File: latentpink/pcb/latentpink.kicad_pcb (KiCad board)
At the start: 8 copper layers, 145 x 139 mm, 470 parts, among them J1 CONN_SFP_HOST, J10 XILINX_JTAG, J13 CONN_01X05, J14 CONN_01X03, J15 CONN_01X03, J16 JUMPER_0402_SPDT, J17 JUMPER_0402_SPDT, J18 BEL_FUSE_0845-2R1T-E4, J19 BEL_FUSE_0845-2R1T-E4, J2 SFP_CAGE, J20 BEL_FUSE_0845-2R1T-E4, J21 BEL_FUSE_0845-2R1T-E4, J22 BEL_FUSE_0845-2R1T-E4, J3 XILINX_JTAG, J4 BEL_FUSE_0845-2R1T-E4, J5 0826-1G1T-23-F, J6 BARREL_JACK, J7 RJ45, J8 BEL_FUSE_0845-2R1T-E4, J9 XILINX_JTAG, M1 960-27-12-D-AB-0, M2 960-23-23-F-AB-0, M3 SCREWHOLE, M4 SCREWHOLE, M5 SCREWHOLE, M6 SCREWHOLE, U1 VSC8512, U10 MYMGK1R812ERSR, U11 MYMGK00504ERSR, U12 STM32L031-QFN32, U13 MYMGK00504ERSR, U14 MYMGK00504ERSR, U15 MYMGK00504ERSR, U16 NCP45521IMNTWG-H, U17 NCP45521IMNTWG-H, U18 LP2996AMRE, U19 TPS7A2533DRVR, U2 XC7K160T-2FBG484C, U20 AT24MAC402, U21 ECX2-LMV-3CN-125.000-TR, U22 ECS-2016MVQ-250-CN, U3 CY7C2245KV18-450BZXI, U4 STM32H735-UFBGA176-25, U5 DP83867, U6 DP83867, U9 KSZ9031RN

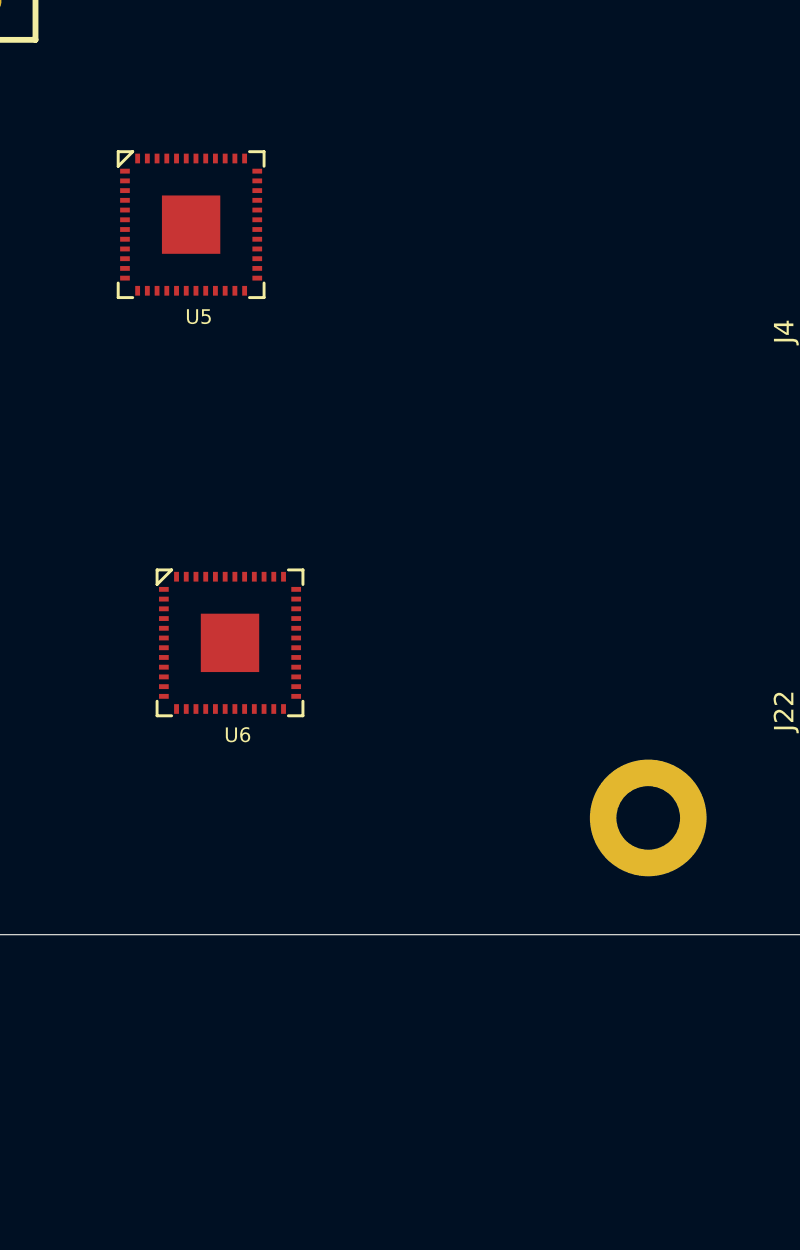
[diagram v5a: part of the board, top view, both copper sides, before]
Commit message: Initial start of DP83867 schematic
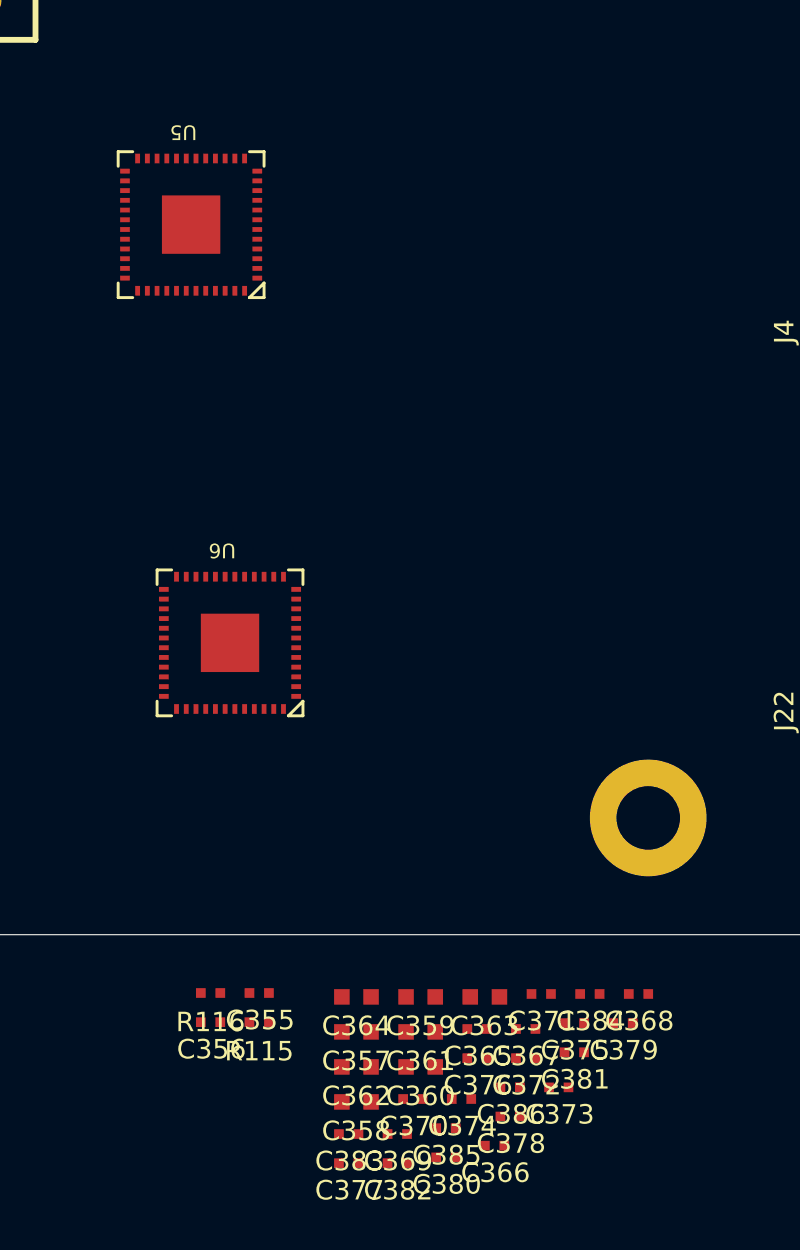
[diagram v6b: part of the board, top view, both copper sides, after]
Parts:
- added C355: 0.47 uF, azonenberg_pcb:EIA_0402_CAP_NOSILK, F.Cu at (121.0, 163.0)
- added C356: 0.47 uF, azonenberg_pcb:EIA_0402_CAP_NOSILK, F.Cu at (118.5, 164.5)
- added C357: 4.7 uF, azonenberg_pcb:EIA_0603_CAP_NOSILK, F.Cu at (126.0, 165.0)
- added C358: 4.7 uF, azonenberg_pcb:EIA_0603_CAP_NOSILK, F.Cu at (126.0, 168.6)
- added C359: 4.7 uF, azonenberg_pcb:EIA_0603_CAP_NOSILK, F.Cu at (129.3, 163.2)
- added C360: 4.7 uF, azonenberg_pcb:EIA_0603_CAP_NOSILK, F.Cu at (129.3, 166.8)
- added C361: 4.7 uF, azonenberg_pcb:EIA_0603_CAP_NOSILK, F.Cu at (129.3, 165.0)
- added C362: 4.7 uF, azonenberg_pcb:EIA_0603_CAP_NOSILK, F.Cu at (126.0, 166.8)
- added C363: 4.7 uF, azonenberg_pcb:EIA_0603_CAP_NOSILK, F.Cu at (132.6, 163.2)
- added C364: 4.7 uF, azonenberg_pcb:EIA_0603_CAP_NOSILK, F.Cu at (126.0, 163.2)
- added C365: 0.47 uF, azonenberg_pcb:EIA_0402_CAP_NOSILK, F.Cu at (132.2, 164.8)
- added C366: 0.47 uF, azonenberg_pcb:EIA_0402_CAP_NOSILK, F.Cu at (133.1, 170.8)
- added C367: 0.47 uF, azonenberg_pcb:EIA_0402_CAP_NOSILK, F.Cu at (134.7, 164.8)
- added C368: 0.47 uF, azonenberg_pcb:EIA_0402_CAP_NOSILK, F.Cu at (140.5, 163.1)
- added C369: 0.47 uF, azonenberg_pcb:EIA_0402_CAP_NOSILK, F.Cu at (128.1, 170.2)
- added C370: 0.47 uF, azonenberg_pcb:EIA_0402_CAP_NOSILK, F.Cu at (128.9, 168.4)
- added C371: 0.47 uF, azonenberg_pcb:EIA_0402_CAP_NOSILK, F.Cu at (135.5, 163.1)
- added C372: 0.47 uF, azonenberg_pcb:EIA_0402_CAP_NOSILK, F.Cu at (134.7, 166.3)
- added C373: 0.47 uF, azonenberg_pcb:EIA_0402_CAP_NOSILK, F.Cu at (136.4, 167.8)
- added C374: 0.47 uF, azonenberg_pcb:EIA_0402_CAP_NOSILK, F.Cu at (131.4, 168.4)
- added C375: 0.47 uF, azonenberg_pcb:EIA_0402_CAP_NOSILK, F.Cu at (137.2, 164.6)
- added C376: 0.47 uF, azonenberg_pcb:EIA_0402_CAP_NOSILK, F.Cu at (132.2, 166.3)
- added C377: 0.47 uF, azonenberg_pcb:EIA_0402_CAP_NOSILK, F.Cu at (125.6, 171.8)
- added C378: 0.47 uF, azonenberg_pcb:EIA_0402_CAP_NOSILK, F.Cu at (133.9, 169.3)
- added C379: 0.47 uF, azonenberg_pcb:EIA_0402_CAP_NOSILK, F.Cu at (139.7, 164.6)
- added C380: 0.47 uF, azonenberg_pcb:EIA_0402_CAP_NOSILK, F.Cu at (130.6, 171.4)
- added C381: 0.47 uF, azonenberg_pcb:EIA_0402_CAP_NOSILK, F.Cu at (137.2, 166.1)
- added C382: 0.47 uF, azonenberg_pcb:EIA_0402_CAP_NOSILK, F.Cu at (128.1, 171.8)
- added C383: 0.47 uF, azonenberg_pcb:EIA_0402_CAP_NOSILK, F.Cu at (125.6, 170.2)
- added C384: 0.47 uF, azonenberg_pcb:EIA_0402_CAP_NOSILK, F.Cu at (138.0, 163.1)
- added C385: 0.47 uF, azonenberg_pcb:EIA_0402_CAP_NOSILK, F.Cu at (130.6, 169.9)
- added C386: 0.47 uF, azonenberg_pcb:EIA_0402_CAP_NOSILK, F.Cu at (133.9, 167.8)
- added R115: 33, azonenberg_pcb:EIA_0402_RES_NOSILK, F.Cu at (121.0, 164.5)
- added R116: 33, azonenberg_pcb:EIA_0402_RES_NOSILK, F.Cu at (118.5, 163.0)
- turned U5 to 180 degrees
- turned U6 to 180 degrees
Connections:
- J18 pad SHLD: /QSGMII PHY/CHGND -> /CHGND
- J19 pad SHLD: /QSGMII PHY/CHGND -> /CHGND
- J20 pad SHLD: /QSGMII PHY/CHGND -> /CHGND
- J21 pad SHLD: /QSGMII PHY/CHGND -> /CHGND
- J22 pad 1: unconnected-(J22-Pad1) -> /GND
- J22 pad 10: unconnected-(J22-Pad10) -> /SGMII PHYs/ETH13_C_N
- J22 pad 11: unconnected-(J22-Pad11) -> /SGMII PHYs/ETH13_B_P
- J22 pad 13: unconnected-(J22-Pad13) -> /SGMII PHYs/ETH13_A_N
- J22 pad 15: unconnected-(J22-Pad15) -> /SGMII PHYs/ETH12_A_N
- J22 pad 16: unconnected-(J22-Pad16) -> /SGMII PHYs/ETH12_B_N
- J22 pad 18: unconnected-(J22-Pad18) -> /SGMII PHYs/ETH12_C_P
- J22 pad 19: unconnected-(J22-Pad19) -> /SGMII PHYs/ETH12_D_N
- J22 pad 2: unconnected-(J22-Pad2) -> /SGMII PHYs/ETH13_D_N
- J22 pad 20: unconnected-(J22-Pad20) -> /GND
- J22 pad 21: unconnected-(J22-Pad21) -> /SGMII PHYs/ETH12_A_N
- J22 pad 23: unconnected-(J22-Pad23) -> /SGMII PHYs/ETH12_B_P
- J22 pad 24: unconnected-(J22-Pad24) -> /SGMII PHYs/ETH12_C_N
- J22 pad 26: unconnected-(J22-Pad26) -> /SGMII PHYs/ETH12_D_P
- J22 pad 3: unconnected-(J22-Pad3) -> /SGMII PHYs/ETH13_C_P
- J22 pad 5: unconnected-(J22-Pad5) -> /SGMII PHYs/ETH13_B_N
- J22 pad 6: unconnected-(J22-Pad6) -> /SGMII PHYs/ETH13_A_P
- J22 pad 9: unconnected-(J22-Pad9) -> /SGMII PHYs/ETH13_D_P
- J22 pad SHLD: unconnected-(J22-PadSHLD) -> /CHGND
- J4 pad SHLD: /QSGMII PHY/CHGND -> /CHGND
- J8 pad SHLD: /QSGMII PHY/CHGND -> /CHGND
- U2 pad AA5: unconnected-(U2-PadAA5) -> /SGMII PHYs/ETH13_INT_N
- U2 pad AA6: unconnected-(U2-PadAA6) -> /SGMII PHYs/DP_MDC
- U2 pad AB5: unconnected-(U2-PadAB5) -> /SGMII PHYs/ETH13_RST_N
- U2 pad AB6: unconnected-(U2-PadAB6) -> /SGMII PHYs/DP_MDIO
- U2 pad AB7: unconnected-(U2-PadAB7) -> /SGMII PHYs/ETH12_RST_N
- U2 pad AB8: unconnected-(U2-PadAB8) -> /SGMII PHYs/ETH12_INT_N
- U2 pad T14: unconnected-(U2-PadT14) -> Net-(U2-PadT14)
- U2 pad T6: unconnected-(U2-PadT6) -> Net-(U2-PadT6)
- U5 pad 1: unconnected-(U5-Pad1) -> /SGMII PHYs/ETH13_A_P
- U5 pad 10: unconnected-(U5-Pad10) -> /SGMII PHYs/ETH13_D_P
- U5 pad 11: unconnected-(U5-Pad11) -> /SGMII PHYs/ETH13_D_N
- U5 pad 12: unconnected-(U5-Pad12) -> Net-(U5-Pad12)
- U5 pad 13: unconnected-(U5-Pad13) -> /SGMII PHYs/DP_A1V8
- U5 pad 15: unconnected-(U5-Pad15) -> /SGMII PHYs/PHY_CLK_25MHZ_1
- U5 pad 16: unconnected-(U5-Pad16) -> /SGMII PHYs/DP_MDC
- U5 pad 17: unconnected-(U5-Pad17) -> /SGMII PHYs/DP_MDIO
- U5 pad 18: unconnected-(U5-Pad18) -> /SGMII PHYs/DP_CLKOUT1
- U5 pad 19: unconnected-(U5-Pad19) -> /1V8
- U5 pad 2: unconnected-(U5-Pad2) -> /SGMII PHYs/ETH13_A_N
- U5 pad 24: unconnected-(U5-Pad24) -> /1V0
- U5 pad 27: unconnected-(U5-Pad27) -> /SGMII PHYs/ETH13_SGMII_TX_P
- U5 pad 28: unconnected-(U5-Pad28) -> /SGMII PHYs/ETH13_SGMII_TX_N
- U5 pad 3: unconnected-(U5-Pad3) -> /SGMII PHYs/DP_A2V5
- U5 pad 30: unconnected-(U5-Pad30) -> /1V8
- U5 pad 31: unconnected-(U5-Pad31) -> /1V0
- U5 pad 33: unconnected-(U5-Pad33) -> /SGMII PHYs/ETH13_SGMII_CLKOUT_P
- U5 pad 34: unconnected-(U5-Pad34) -> /SGMII PHYs/ETH13_SGMII_CLKOUT_N
- U5 pad 35: unconnected-(U5-Pad35) -> /SGMII PHYs/ETH13_SGMII_RX_P
- U5 pad 36: unconnected-(U5-Pad36) -> /SGMII PHYs/ETH13_SGMII_RX_N
- U5 pad 38: unconnected-(U5-Pad38) -> /SGMII PHYs/ETH13_RX_CTRL_STRAP
- U5 pad 4: unconnected-(U5-Pad4) -> /SGMII PHYs/ETH13_B_P
- U5 pad 41: unconnected-(U5-Pad41) -> /1V8
- U5 pad 42: unconnected-(U5-Pad42) -> /1V0
- U5 pad 43: unconnected-(U5-Pad43) -> /SGMII PHYs/ETH13_RST_N
- U5 pad 44: unconnected-(U5-Pad44) -> /SGMII PHYs/ETH13_INT_N
- U5 pad 48: unconnected-(U5-Pad48) -> /SGMII PHYs/DP_A1V8
- U5 pad 5: unconnected-(U5-Pad5) -> /SGMII PHYs/ETH13_B_N
- U5 pad 6: unconnected-(U5-Pad6) -> /1V0
- U5 pad 7: unconnected-(U5-Pad7) -> /SGMII PHYs/ETH13_C_P
- U5 pad 8: unconnected-(U5-Pad8) -> /SGMII PHYs/ETH13_C_N
- U5 pad 9: unconnected-(U5-Pad9) -> /SGMII PHYs/DP_A2V5
- U5 pad PAD: unconnected-(U5-PadPAD) -> /GND
- U6 pad 1: unconnected-(U6-Pad1) -> /SGMII PHYs/ETH12_A_P
- U6 pad 10: unconnected-(U6-Pad10) -> /SGMII PHYs/ETH12_D_P
- U6 pad 11: unconnected-(U6-Pad11) -> /SGMII PHYs/ETH12_D_N
- U6 pad 12: unconnected-(U6-Pad12) -> Net-(U6-Pad12)
- U6 pad 13: unconnected-(U6-Pad13) -> /SGMII PHYs/DP_A1V8
- U6 pad 15: unconnected-(U6-Pad15) -> /SGMII PHYs/PHY_CLK_25MHZ_0
- U6 pad 16: unconnected-(U6-Pad16) -> /SGMII PHYs/DP_MDC
- U6 pad 17: unconnected-(U6-Pad17) -> /SGMII PHYs/DP_MDIO
- U6 pad 18: unconnected-(U6-Pad18) -> /SGMII PHYs/DP_CLKOUT0
- U6 pad 19: unconnected-(U6-Pad19) -> /1V8
- U6 pad 2: unconnected-(U6-Pad2) -> /SGMII PHYs/ETH12_A_N
- U6 pad 24: unconnected-(U6-Pad24) -> /1V0
- U6 pad 27: unconnected-(U6-Pad27) -> /SGMII PHYs/ETH12_SGMII_TX_P
- U6 pad 28: unconnected-(U6-Pad28) -> /SGMII PHYs/ETH12_SGMII_TX_N
- U6 pad 3: unconnected-(U6-Pad3) -> /SGMII PHYs/DP_A2V5
- U6 pad 30: unconnected-(U6-Pad30) -> /1V8
- U6 pad 31: unconnected-(U6-Pad31) -> /1V0
- U6 pad 33: unconnected-(U6-Pad33) -> /SGMII PHYs/ETH12_SGMII_CLKOUT_P
- U6 pad 34: unconnected-(U6-Pad34) -> /SGMII PHYs/ETH12_SGMII_CLKOUT_N
- U6 pad 35: unconnected-(U6-Pad35) -> /SGMII PHYs/ETH12_SGMII_RX_P
- U6 pad 36: unconnected-(U6-Pad36) -> /SGMII PHYs/ETH12_SGMII_RX_N
- U6 pad 38: unconnected-(U6-Pad38) -> /SGMII PHYs/ETH12_RX_CTRL_STRAP
- U6 pad 4: unconnected-(U6-Pad4) -> /SGMII PHYs/ETH12_B_P
- U6 pad 41: unconnected-(U6-Pad41) -> /1V8
- U6 pad 42: unconnected-(U6-Pad42) -> /1V0
- U6 pad 43: unconnected-(U6-Pad43) -> /SGMII PHYs/ETH12_RST_N
- U6 pad 44: unconnected-(U6-Pad44) -> /SGMII PHYs/ETH12_INT_N
- U6 pad 48: unconnected-(U6-Pad48) -> /SGMII PHYs/DP_A1V8
- U6 pad 5: unconnected-(U6-Pad5) -> /SGMII PHYs/ETH12_B_N
- U6 pad 6: unconnected-(U6-Pad6) -> /1V0
- U6 pad 7: unconnected-(U6-Pad7) -> /SGMII PHYs/ETH12_C_P
- U6 pad 8: unconnected-(U6-Pad8) -> /SGMII PHYs/ETH12_C_N
- U6 pad 9: unconnected-(U6-Pad9) -> /SGMII PHYs/DP_A2V5
- U6 pad PAD: unconnected-(U6-PadPAD) -> /GND

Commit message: Rearranged ports, added center tap capacitors
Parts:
- added C387: 0.1 uF, azonenberg_pcb:EIA_0402_CAP_NOSILK, F.Cu at (118.5, 47.0)
- added C388: 0.1 uF, azonenberg_pcb:EIA_0402_CAP_NOSILK, F.Cu at (113.5, 47.0)
- added C389: 0.1 uF, azonenberg_pcb:EIA_0402_CAP_NOSILK, F.Cu at (113.5, 48.5)
- added C390: 0.1 uF, azonenberg_pcb:EIA_0402_CAP_NOSILK, F.Cu at (116.0, 48.5)
- added C391: 0.1 uF, azonenberg_pcb:EIA_0402_CAP_NOSILK, F.Cu at (116.0, 47.0)
- added C392: 0.1 uF, azonenberg_pcb:EIA_0402_CAP_NOSILK, F.Cu at (118.5, 48.5)
- added C393: 0.1 uF, azonenberg_pcb:EIA_0402_CAP_NOSILK, F.Cu at (202.5, 31.0)
- added C394: 0.1 uF, azonenberg_pcb:EIA_0402_CAP_NOSILK, F.Cu at (195.0, 31.0)
- added C395: 0.1 uF, azonenberg_pcb:EIA_0402_CAP_NOSILK, F.Cu at (192.5, 34.0)
- added C396: 0.1 uF, azonenberg_pcb:EIA_0402_CAP_NOSILK, F.Cu at (207.5, 26.5)
- added C397: 0.1 uF, azonenberg_pcb:EIA_0402_CAP_NOSILK, F.Cu at (192.5, 32.5)
- added C398: 0.1 uF, azonenberg_pcb:EIA_0402_CAP_NOSILK, F.Cu at (192.5, 26.5)
- added C399: 0.1 uF, azonenberg_pcb:EIA_0402_CAP_NOSILK, F.Cu at (195.0, 28.0)
- added C400: 0.1 uF, azonenberg_pcb:EIA_0402_CAP_NOSILK, F.Cu at (200.0, 32.5)
- added C401: 0.1 uF, azonenberg_pcb:EIA_0402_CAP_NOSILK, F.Cu at (205.0, 26.5)
- added C402: 0.1 uF, azonenberg_pcb:EIA_0402_CAP_NOSILK, F.Cu at (197.5, 35.5)
- added C403: 0.1 uF, azonenberg_pcb:EIA_0402_CAP_NOSILK, F.Cu at (197.5, 32.5)
- added C404: 0.1 uF, azonenberg_pcb:EIA_0402_CAP_NOSILK, F.Cu at (202.5, 34.0)
- added C405: 0.1 uF, azonenberg_pcb:EIA_0402_CAP_NOSILK, F.Cu at (200.0, 29.5)
- added C406: 0.1 uF, azonenberg_pcb:EIA_0402_CAP_NOSILK, F.Cu at (195.0, 34.0)
- added C407: 0.1 uF, azonenberg_pcb:EIA_0402_CAP_NOSILK, F.Cu at (197.5, 31.0)
- added C408: 0.1 uF, azonenberg_pcb:EIA_0402_CAP_NOSILK, F.Cu at (197.5, 26.5)
- added C409: 0.1 uF, azonenberg_pcb:EIA_0402_CAP_NOSILK, F.Cu at (205.0, 28.0)
- added C410: 0.1 uF, azonenberg_pcb:EIA_0402_CAP_NOSILK, F.Cu at (195.0, 26.5)
- added C411: 0.1 uF, azonenberg_pcb:EIA_0402_CAP_NOSILK, F.Cu at (200.0, 28.0)
- added C412: 0.1 uF, azonenberg_pcb:EIA_0402_CAP_NOSILK, F.Cu at (195.0, 35.5)
- added C413: 0.1 uF, azonenberg_pcb:EIA_0402_CAP_NOSILK, F.Cu at (197.5, 37.0)
- added C414: 0.1 uF, azonenberg_pcb:EIA_0402_CAP_NOSILK, F.Cu at (200.0, 34.0)
- added C415: 0.1 uF, azonenberg_pcb:EIA_0402_CAP_NOSILK, F.Cu at (195.0, 37.0)
- added C416: 0.1 uF, azonenberg_pcb:EIA_0402_CAP_NOSILK, F.Cu at (202.5, 28.0)
- added C417: 0.1 uF, azonenberg_pcb:EIA_0402_CAP_NOSILK, F.Cu at (207.5, 28.0)
- added C418: 0.1 uF, azonenberg_pcb:EIA_0402_CAP_NOSILK, F.Cu at (195.0, 29.5)
- added C419: 0.1 uF, azonenberg_pcb:EIA_0402_CAP_NOSILK, F.Cu at (205.0, 31.0)
- added C420: 0.1 uF, azonenberg_pcb:EIA_0402_CAP_NOSILK, F.Cu at (192.5, 28.0)
- added C421: 0.1 uF, azonenberg_pcb:EIA_0402_CAP_NOSILK, F.Cu at (192.5, 35.5)
- added C422: 0.1 uF, azonenberg_pcb:EIA_0402_CAP_NOSILK, F.Cu at (210.0, 26.5)
- added C423: 0.1 uF, azonenberg_pcb:EIA_0402_CAP_NOSILK, F.Cu at (192.5, 29.5)
- added C424: 0.1 uF, azonenberg_pcb:EIA_0402_CAP_NOSILK, F.Cu at (192.5, 31.0)
- added C425: 0.1 uF, azonenberg_pcb:EIA_0402_CAP_NOSILK, F.Cu at (202.5, 29.5)
- added C426: 0.1 uF, azonenberg_pcb:EIA_0402_CAP_NOSILK, F.Cu at (202.5, 32.5)
- added C427: 0.1 uF, azonenberg_pcb:EIA_0402_CAP_NOSILK, F.Cu at (197.5, 29.5)
- added C428: 0.1 uF, azonenberg_pcb:EIA_0402_CAP_NOSILK, F.Cu at (205.0, 29.5)
- added C429: 0.1 uF, azonenberg_pcb:EIA_0402_CAP_NOSILK, F.Cu at (197.5, 34.0)
- added C430: 0.1 uF, azonenberg_pcb:EIA_0402_CAP_NOSILK, F.Cu at (197.5, 28.0)
- added C431: 0.1 uF, azonenberg_pcb:EIA_0402_CAP_NOSILK, F.Cu at (207.5, 29.5)
- added C432: 0.1 uF, azonenberg_pcb:EIA_0402_CAP_NOSILK, F.Cu at (210.0, 28.0)
- added C433: 0.1 uF, azonenberg_pcb:EIA_0402_CAP_NOSILK, F.Cu at (202.5, 26.5)
- added C434: 0.1 uF, azonenberg_pcb:EIA_0402_CAP_NOSILK, F.Cu at (205.0, 32.5)
- added C435: 0.1 uF, azonenberg_pcb:EIA_0402_CAP_NOSILK, F.Cu at (192.5, 37.0)
- added C436: 0.1 uF, azonenberg_pcb:EIA_0402_CAP_NOSILK, F.Cu at (200.0, 35.5)
- added C437: 0.1 uF, azonenberg_pcb:EIA_0402_CAP_NOSILK, F.Cu at (195.0, 32.5)
- added C438: 0.1 uF, azonenberg_pcb:EIA_0402_CAP_NOSILK, B.Cu at (153.8, 54.5)
- added C439: 0.1 uF, azonenberg_pcb:EIA_0402_CAP_NOSILK, F.Cu at (200.0, 37.0)
- added C440: 0.1 uF, azonenberg_pcb:EIA_0402_CAP_NOSILK, B.Cu at (153.8, 48.5)
- added U23: ADM3101E_QFN, azonenberg_pcb:QFN_12_0.5MM_3x3MM, F.Cu at (64.0, 70.0)
- R100, R103, R82, R85, R87, R90, R91, R94, R99: moved to B.Cu
- moved J15 193.2 mm to (76.5, 136.5)
- moved C360 141.1 mm to (110.2, 26.9)
- moved C362 141.1 mm to (106.9, 26.9)
- moved C368 141.1 mm to (121.4, 23.2)
- moved C371 141.1 mm to (116.4, 23.2)
- moved C375 141.1 mm to (118.1, 24.7)
- moved C379 141.1 mm to (120.6, 24.7)
- moved C381 141.1 mm to (118.1, 26.2)
- moved C384 141.1 mm to (118.9, 23.2)
- moved C355 141.1 mm to (101.9, 23.1)
- moved C356 141.1 mm to (99.4, 24.6)
- moved C357 141.1 mm to (106.9, 25.1)
- moved C358 141.1 mm to (106.9, 28.8)
- moved C359 141.1 mm to (110.2, 23.4)
- moved C361 141.1 mm to (110.2, 25.1)
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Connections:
- C355 pad 1: /1V8 -> /SGMII PHYs/1V8_IO
- C356 pad 1: /1V8 -> /SGMII PHYs/1V8_IO
- C360 pad 1: /SGMII PHYs/D1V8 -> /SGMII PHYs/1V8_IO
- C364 pad 1: /SGMII PHYs/D1V8 -> /SGMII PHYs/1V8_IO
- C368 pad 1: /SGMII PHYs/D1V8 -> /SGMII PHYs/1V8_IO
- C372 pad 1: /SGMII PHYs/D1V8 -> /SGMII PHYs/1V8_IO
- C375 pad 1: /SGMII PHYs/D1V8 -> /SGMII PHYs/1V8_IO
- C378 pad 1: /SGMII PHYs/D1V8 -> /SGMII PHYs/1V8_IO
- C382 pad 1: /SGMII PHYs/D1V8 -> /SGMII PHYs/1V8_IO
- C384 pad 1: /SGMII PHYs/D1V8 -> /SGMII PHYs/1V8_IO
- J18 pad 12: unconnected-(J18-Pad12) -> /QSGMII PHY/ETH4_TAP_1
- J18 pad 14: unconnected-(J18-Pad14) -> /QSGMII PHY/ETH5_TAP_0
- J18 pad 17: unconnected-(J18-Pad17) -> /QSGMII PHY/ETH5_TAP_2
- J18 pad 22: unconnected-(J18-Pad22) -> /QSGMII PHY/ETH5_TAP_1
- J18 pad 25: unconnected-(J18-Pad25) -> /QSGMII PHY/ETH5_TAP_3
- J18 pad 4: unconnected-(J18-Pad4) -> /QSGMII PHY/ETH4_TAP_2
- J18 pad 7: unconnected-(J18-Pad7) -> /QSGMII PHY/ETH4_TAP_0
- J18 pad 8: unconnected-(J18-Pad8) -> /QSGMII PHY/ETH4_TAP_3
- J19 pad 12: unconnected-(J19-Pad12) -> /QSGMII PHY/ETH6_TAP_1
- J19 pad 14: unconnected-(J19-Pad14) -> /QSGMII PHY/ETH7_TAP_0
- J19 pad 17: unconnected-(J19-Pad17) -> /QSGMII PHY/ETH7_TAP_2
- J19 pad 22: unconnected-(J19-Pad22) -> /QSGMII PHY/ETH7_TAP_1
- J19 pad 25: unconnected-(J19-Pad25) -> /QSGMII PHY/ETH7_TAP_3
- J19 pad 4: unconnected-(J19-Pad4) -> /QSGMII PHY/ETH6_TAP_2
- J19 pad 7: unconnected-(J19-Pad7) -> /QSGMII PHY/ETH6_TAP_0
- J19 pad 8: unconnected-(J19-Pad8) -> /QSGMII PHY/ETH6_TAP_3
- J20 pad 12: unconnected-(J20-Pad12) -> /QSGMII PHY/ETH8_TAP_1
- J20 pad 14: unconnected-(J20-Pad14) -> /QSGMII PHY/ETH9_TAP_0
- J20 pad 17: unconnected-(J20-Pad17) -> /QSGMII PHY/ETH9_TAP_2
- J20 pad 22: unconnected-(J20-Pad22) -> /QSGMII PHY/ETH9_TAP_1
- J20 pad 25: unconnected-(J20-Pad25) -> /QSGMII PHY/ETH9_TAP_3
- J20 pad 4: unconnected-(J20-Pad4) -> /QSGMII PHY/ETH8_TAP_2
- J20 pad 7: unconnected-(J20-Pad7) -> /QSGMII PHY/ETH8_TAP_0
- J20 pad 8: unconnected-(J20-Pad8) -> /QSGMII PHY/ETH8_TAP_3
- J21 pad 12: unconnected-(J21-Pad12) -> /QSGMII PHY/ETH10_TAP_1
- J21 pad 14: unconnected-(J21-Pad14) -> /QSGMII PHY/ETH11_TAP_0
- J21 pad 17: unconnected-(J21-Pad17) -> /QSGMII PHY/ETH11_TAP_2
- J21 pad 22: unconnected-(J21-Pad22) -> /QSGMII PHY/ETH11_TAP_1
- J21 pad 25: unconnected-(J21-Pad25) -> /QSGMII PHY/ETH11_TAP_3
- J21 pad 4: unconnected-(J21-Pad4) -> /QSGMII PHY/ETH10_TAP_2
- J21 pad 7: unconnected-(J21-Pad7) -> /QSGMII PHY/ETH10_TAP_0
- J21 pad 8: unconnected-(J21-Pad8) -> /QSGMII PHY/ETH10_TAP_3
- J4 pad 12: unconnected-(J4-Pad12) -> /QSGMII PHY/ETH0_TAP_1
- J4 pad 14: unconnected-(J4-Pad14) -> /QSGMII PHY/ETH1_TAP_0
- J4 pad 17: unconnected-(J4-Pad17) -> /QSGMII PHY/ETH1_TAP_2
- J4 pad 22: unconnected-(J4-Pad22) -> /QSGMII PHY/ETH1_TAP_1
- J4 pad 25: unconnected-(J4-Pad25) -> /QSGMII PHY/ETH1_TAP_3
- J4 pad 4: unconnected-(J4-Pad4) -> /QSGMII PHY/ETH0_TAP_2
- J4 pad 7: unconnected-(J4-Pad7) -> /QSGMII PHY/ETH0_TAP_0
- J4 pad 8: unconnected-(J4-Pad8) -> /QSGMII PHY/ETH0_TAP_3
- J8 pad 12: unconnected-(J8-Pad12) -> /QSGMII PHY/ETH2_TAP_1
- J8 pad 14: unconnected-(J8-Pad14) -> /QSGMII PHY/ETH3_TAP_0
- J8 pad 17: unconnected-(J8-Pad17) -> /QSGMII PHY/ETH3_TAP_2
- J8 pad 22: unconnected-(J8-Pad22) -> /QSGMII PHY/ETH3_TAP_1
- J8 pad 25: unconnected-(J8-Pad25) -> /QSGMII PHY/ETH3_TAP_3
- J8 pad 4: unconnected-(J8-Pad4) -> /QSGMII PHY/ETH2_TAP_2
- J8 pad 7: unconnected-(J8-Pad7) -> /QSGMII PHY/ETH2_TAP_0
- J8 pad 8: unconnected-(J8-Pad8) -> /QSGMII PHY/ETH2_TAP_3
- U2 pad U6: unconnected-(U2-PadU6) -> /SGMII PHYs/ETH12_SGMII_RX_AC_N
- U2 pad U7: unconnected-(U2-PadU7) -> /SGMII PHYs/ETH12_SGMII_RX_AC_P
- U2 pad V7: unconnected-(U2-PadV7) -> /SGMII PHYs/ETH12_SGMII_TX_AC_P
- U2 pad W7: unconnected-(U2-PadW7) -> /SGMII PHYs/ETH12_SGMII_TX_AC_N
- U2 pad Y7: unconnected-(U2-PadY7) -> /SGMII PHYs/ETH12_SGMII_CLKOUT_AC_N
- U2 pad Y8: unconnected-(U2-PadY8) -> /SGMII PHYs/ETH12_SGMII_CLKOUT_AC_P
- U5 pad 19: /1V8 -> /SGMII PHYs/1V8_IO
- U5 pad 30: /1V8 -> /SGMII PHYs/1V8_IO
- U5 pad 41: /1V8 -> /SGMII PHYs/1V8_IO
- U6 pad 19: /1V8 -> /SGMII PHYs/1V8_IO
- U6 pad 30: /1V8 -> /SGMII PHYs/1V8_IO
- U6 pad 41: /1V8 -> /SGMII PHYs/1V8_IO
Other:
- board text added: "3V3_SB"
- board text added: "FPGA JTAG 1.8V"
- board text added: "GND"
- board text added: "MCU JTAG 3.3V"
- board text added: "PHY JTAG 2.5V"
- board text added: "RST#"
- board text added: "RX"
- board text added: "SUPER SWD 3.3V"
- board text added: "SUPER UART 3.3V"
- board text added: "SWCLK"
- board text added: "SWDIO"
- board text added: "TX"

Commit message: Continued initial component placement
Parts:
- removed C229: 0.1 uF, azonenberg_pcb:EIA_0402_CAP_NOSILK
- removed R53: 1M, azonenberg_pcb:EIA_0402_RES_NOSILK
- added C441: 0.1 uF, azonenberg_pcb:EIA_0402_CAP_NOSILK, F.Cu at (122.4, 51.1)
- added C442: 0.1 uF, azonenberg_pcb:EIA_0402_CAP_NOSILK, F.Cu at (122.4, 51.9)
- added C443: 0.1 uF, azonenberg_pcb:EIA_0402_CAP_NOSILK, F.Cu at (119.8, 54.1)
- added C444: 0.1 uF, azonenberg_pcb:EIA_0402_CAP_NOSILK, F.Cu at (119.8, 54.9)
- added C445: 0.1 uF, azonenberg_pcb:EIA_0402_CAP_NOSILK, F.Cu at (122.4, 55.1)
- added C446: 0.1 uF, azonenberg_pcb:EIA_0402_CAP_NOSILK, F.Cu at (122.4, 55.9)
- C10, C11, C134, C14, C15, C16, C162, C163, C164, C165, C166, C17, C18, C19, C2, C207, C21, C211, C212, C213, C215, C216, C219, C22, C220, C222, C223, C224, C225, C23, C235, C236, C237, C238, C25, C27, C276, C278, C28, C285, C288, C29, C295, C297, C299, C3, C30, C306, C307, C31, C311, C312, C317, C322, C33, C34, C35, C36, C38, C39, C393, C394, C395, C396, C397, C398, C399, C4, C40, C400, C401, C402, C403, C404, C405, C406, C407, C408, C409, C41, C410, C411, C412, C413, C414, C415, C416, C417, C418, C419, C42, C420, C421, C422, C423, C424, C425, C426, C427, C428, C429, C43, C430, C431, C432, C433, C434, C435, C436, C437, C439, C44, C45, C46, C47, C48, C49, C5, C50, C51, C52, C54, C55, C56, C57, C58, C59, C60, C61, C62, C64, C65, C66, C69, C7, C72, C73, C74, C76, C77, C78, C79, C8, C80, C82, C83, C84, C87, C88, C9, R101, R102, R104, R54, R55, R81, R83, R84, R86, R88, R89, R92, R93, R95, R96, R97, R98: moved to B.Cu
- moved TP16 205.6 mm to (26.8, 143.0)
- moved C257 185.6 mm to (67.0, 64.2)
- moved J16 185.6 mm to (64.0, 65.8)
- moved J17 185.6 mm to (64.0, 64.2)
- moved R6 160.9 mm to (89.2, 29.2)
- moved R5 156.0 mm to (91.8, 29.0)
- moved R2 136.4 mm to (96.2, 58.8)
- moved C396 134.6 mm to (164.2, 154.0)
- moved C398 131.3 mm to (153.7, 152.0)
- moved C397 126.7 mm to (160.0, 155.0), turned to 180 degrees
- moved C399 126.0 mm to (160.0, 149.0), turned to 180 degrees
- moved C295 124.4 mm to (116.0, 98.7), turned to -90 degrees
- moved C400 122.6 mm to (153.8, 146.0)
- moved C299 120.3 mm to (115.5, 89.2), turned to 180 degrees
- moved C394 119.0 mm to (164.3, 146.0)
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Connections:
- C210 pad 1: /Management/VDDA -> /Management/MCU_VDDA
- C213 pad 1: /Management/VDDA -> /Management/MCU_VDDA
- FB5 pad 2: /Management/VDDA -> /Management/MCU_VDDA
- J5 pad 17: Net-(C229-Pad2) -> /CHGND
